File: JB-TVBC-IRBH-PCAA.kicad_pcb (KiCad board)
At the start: 2 copper layers, 65 x 56 mm, 70 parts, among them J1 CONN_2x20_FEM_100PITCH_635INS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, J2 SJ-435107, J3 SJ-435107, J4 SJ-435107, Q1 DMG2305UX-7, Q2 DMG2305UX-7, Q3 DMG2305UX-7, Q4 DMG2305UX-7, Q5 DMG2305UX-7, Q6 DMG2305UX-7, U1 CAT24C32, U2 LTC1693-5, U3 LTC1693-5, U4 LTC1693-5, U5 LTC1693-5, U6 LTC1693-5, U7 LTC1693-5

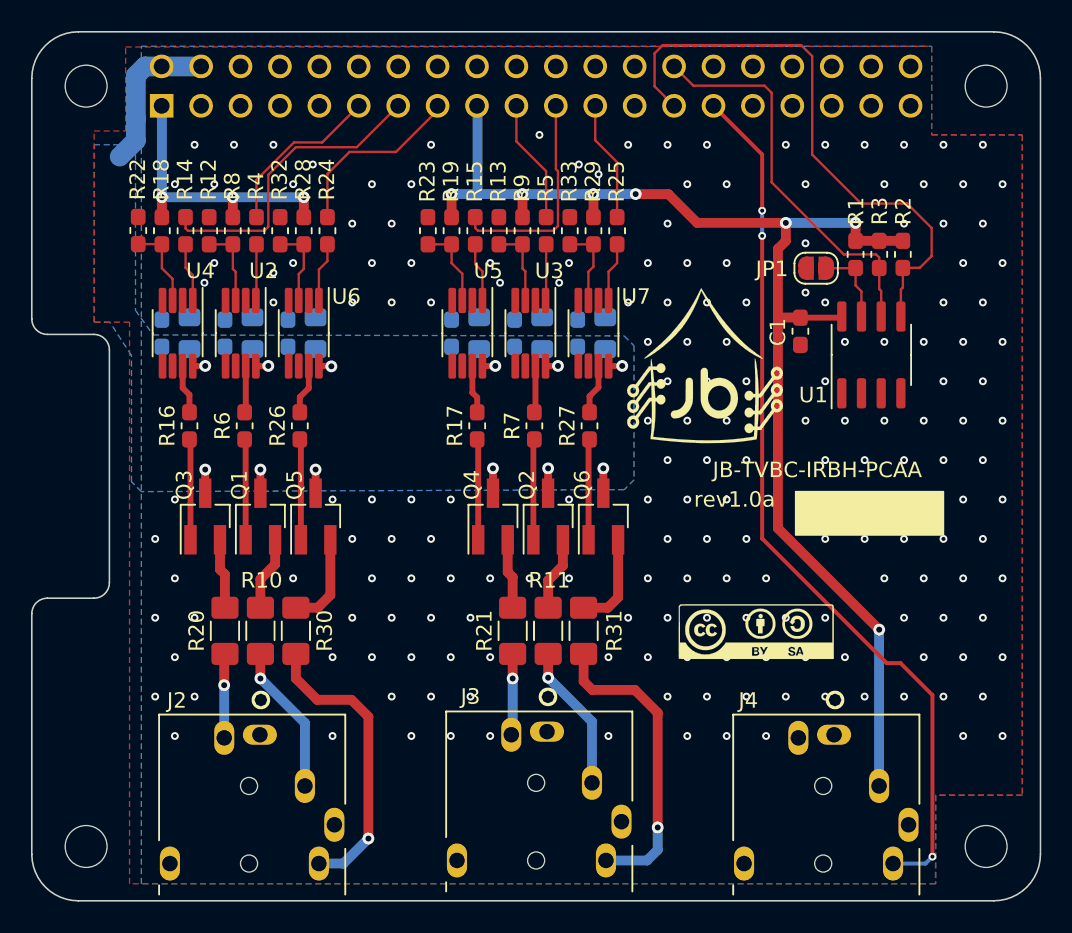
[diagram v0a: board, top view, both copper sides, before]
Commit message: adding fiducial + graphics symbol
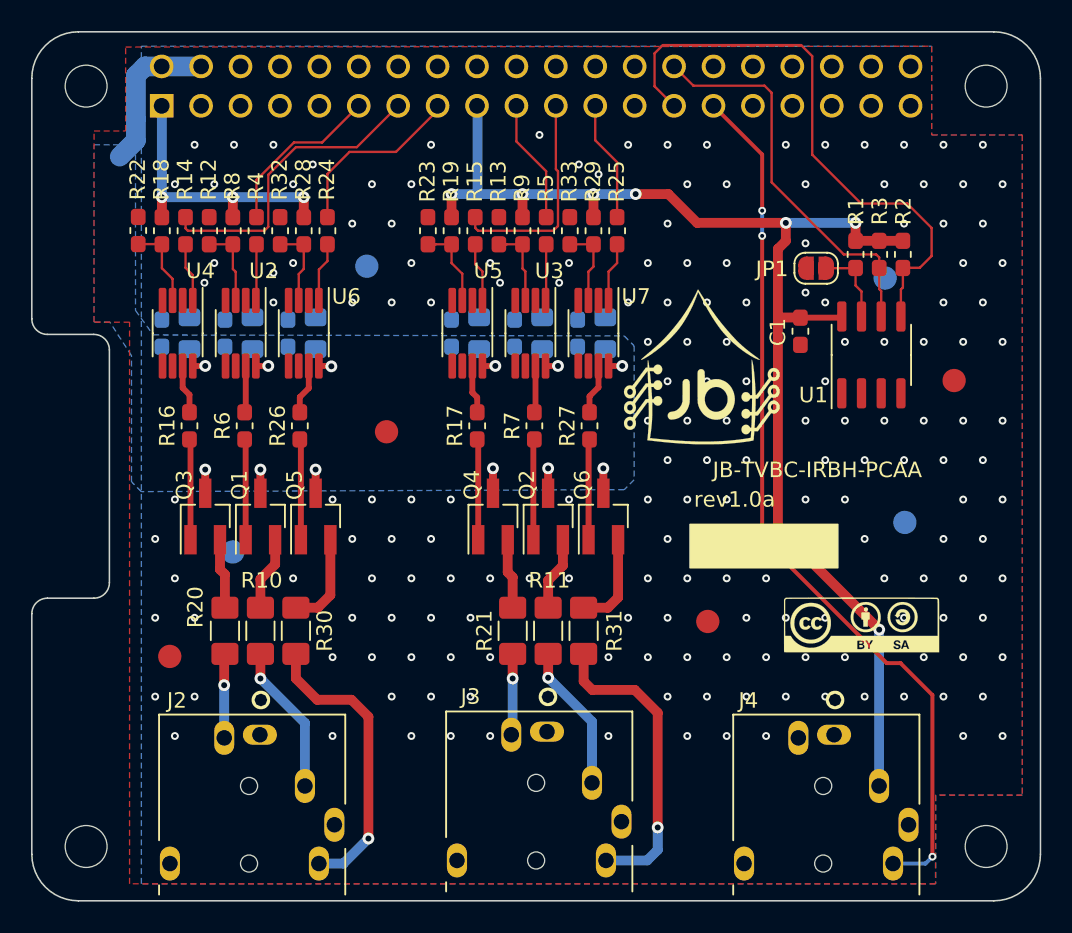
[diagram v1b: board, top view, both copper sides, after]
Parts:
- removed G***: LOGO, JB_Bitmaps:CC-BY-SA_10MM
- removed G***: LOGO, JB_Bitmaps:JB_Logo_10MM
- added FID1: Fiducial, JB_Mechanical:Fiducial_1.5mm_Mask3mm, F.Cu at (122.9, 99.8)
- added FID2: Fiducial, JB_Mechanical:Fiducial_1.5mm_Mask3mm, F.Cu at (108.9, 114.3)
- added FID3: Fiducial, JB_Mechanical:Fiducial_1.5mm_Mask3mm, F.Cu at (143.6, 112.0)
- added FID4: Fiducial, JB_Mechanical:Fiducial_1.5mm_Mask3mm, F.Cu at (159.4, 96.5)
- added FID5: Fiducial, JB_Mechanical:Fiducial_1.5mm_Mask3mm, B.Cu at (121.6, 89.1)
- added FID6: Fiducial, JB_Mechanical:Fiducial_1.5mm_Mask3mm, B.Cu at (155.0, 89.9)
- added FID7: Fiducial, JB_Mechanical:Fiducial_1.5mm_Mask3mm, B.Cu at (113.0, 107.5)
- added FID8: Fiducial, JB_Mechanical:Fiducial_1.5mm_Mask3mm, B.Cu at (156.3, 105.6)
- added G1: JudeBake_Logo, JB_Bitmaps:JB_Logo_10MM, F.Cu at (143.2, 95.6)
- added G2: CC-BY-SA_Logo, JB_Bitmaps:CC-BY-SA_10MM, F.Cu at (153.5, 112.2)
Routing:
- net GND: vias 193 -> 185
